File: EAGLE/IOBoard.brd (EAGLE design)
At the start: 160 x 100 mm, 71 parts, among them IC1 MEGA32-P, IC2 MAX232, IC3 ADM803SAKS, K1 HE3321, K2 HE3321, K3 HE3321, K4 HE3321, K5 HE3321, K6 HE3321, K7 HE3321, K8 HE3321, T1 NDS351AN, T2 NDS351AN, T3 NDS351AN, T4 NDS351AN, T5 NDS351AN, T6 NDS351AN, T7 NDS351AN, T8 NDS351AN

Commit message: -
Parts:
- removed D1, D2, D3, D4, D5, D6, D7, D8: 1N4148, diode:DO35-10
- removed IC2: MAX232, maxim:DIL16
- removed IC3: ADM803SAKS, memmert_joerg:SC70-3L
- removed K1, K2, K3, K4, K5, K6, K7, K8: HE3321, relay:HE3321
- removed OK1, OK2, OK3, OK4, OK5, OK6, OK7, OK8: SFH6206, optocoupler:DIL4-SMD
- removed R10, R11, R12, R13, R14, R15, R16: 374, rcl:0207/10
- removed T1, T2, T3, T4, T5, T6, T7, T8: NDS351AN, memmert_joerg:SOT23
- removed X1, X10, X11, X12, X13, X14, X15, X16, X2, X3, X4, X5, X6, X7, X8, X9: (no value), con-phoenix-500:MSTBV2
- removed X17: (no value), con-subd:F09H
- added 3V3, BAT: (no value), pinhead:1X02
- added C3, C4, C5: 100n, rcl:C0805
- added C6, C7, C8, C9: 20p, rcl:C0805
- added JP1: (no value), pinhead:1X09
- added JP10, JP11, JP2, JP3, JP4, JP5, JP6, JP7, JP8, JP9: JUMPER_SMALL, memmert_joerg:JUMPER
- added JTAG: (no value), con-harting-ml:ML20
- added LED1, LED2, LED3, LED4: (no value), led:SML0603
- added Q2: 32kHz, crystal:MC-306
- added S1: COMBICON_1803442, memmert_joerg:COMBICON_1803442
- added U1: STM32F10XRXT6, stm32:TQFP64
- C1, C2: value (none) -> 100n; device rcl:C025_050-025X075 -> rcl:C0805
- IC1: value MEGA32-P -> TPS61097; device atmel:DIL40 -> spfennig:SOT23-DBV
- Q1: value (none) -> 8MHz; device memmert_joerg:HC49/S -> crystal:CSM-7X-DU
- R1: value 5k -> 390; device rcl:0207/10 -> rcl:R0805
- R2, R3, R4: value 5k -> 10k; device rcl:0207/10 -> rcl:R0805
- R5: value 5k -> 0; device rcl:0207/10 -> rcl:R0805
- R6, R7, R8: value 5k -> 500; device rcl:0207/10 -> rcl:R0805
- R9: value 374 -> 500; device rcl:0207/10 -> rcl:R0805
- moved Q1 299.5 mm to (7.62, 19.7), turned to 90 degrees
- moved C2 237.0 mm to (16.5, 28.6), turned to 270 degrees
- moved C1 217.6 mm to (17.1, 10.8), turned to 90 degrees
- moved R8 150.5 mm to (3.17, 6.99)
- moved R7 130.8 mm to (3.17, 4.45)
- moved R6 111.4 mm to (3.17, 1.91)
- moved IC1 78.0 mm to (2.54, -5.08), turned to 0 degrees
- moved R5 65.5 mm to (27.3, 13.3), turned to 270 degrees
- moved R4 36.1 mm to (36.8, 38.1), turned to 90 degrees
- moved R3 20.1 mm to (34.3, 38.1), turned to 90 degrees
- moved R9 12.6 mm to (3.17, 9.53), turned to 0 degrees
- moved R2 12.0 mm to (26.7, 38.1), turned to 90 degrees
- moved R1 7.10 mm to (11.4, 19.7), turned to 270 degrees
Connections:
- removed net IN0: IC1.40, OK1.4, R1.1
- removed net IN1: IC1.39, OK2.4, R2.1
- removed net IN2: IC1.38, OK3.4, R3.1
- removed net IN3: IC1.37, OK4.4, R4.1
- removed net IN4: IC1.36, OK5.4, R5.1
- removed net IN5: IC1.35, OK6.4, R6.1
- removed net IN6: IC1.34, OK7.4, R7.1
- removed net IN7: IC1.33, OK8.4, R8.1
- removed net N$15: OK3.1, R11.2
- removed net N$16: C2.2, IC2.5
- removed net N$17: R13.1, X5.1
- removed net N$18: OK5.2, X5.2
- removed net N$19: D1.A, K1.3, T1.3
- removed net N$20: OK5.1, R13.2
- removed net N$21: R14.1, X6.1
- removed net N$22: OK6.2, X6.2
- removed net N$23: IC1.9, IC3.2
- removed net N$24: OK6.1, R14.2
- removed net N$25: R15.1, X7.1
- removed net N$26: OK7.2, X7.2
- removed net N$27: D4.A, K2.3, T2.3
- removed net N$28: OK7.1, R15.2
- removed net N$29: R16.1, X8.1
- removed net N$30: OK8.2, X8.2
- removed net N$31: D5.A, K3.3, T3.3
- removed net N$32: OK8.1, R16.2
- removed net N$33: D7.A, K4.3, T4.3
- removed net N$34: D2.A, K5.3, T5.3
- removed net N$35: D3.A, K6.3, T6.3
- removed net N$36: D8.A, K8.3, T8.3
- removed net N$37: D6.A, K7.3, T7.3
- removed net N$38: K1.4, X9.2
- removed net N$39: K1.1, X9.1
- removed net N$40: K2.4, X10.2
- removed net N$41: K2.1, X10.1
- removed net N$42: K3.4, X11.2
- removed net N$43: K3.1, X11.1
- removed net N$44: K4.4, X12.2
- removed net N$45: K4.1, X12.1
- removed net N$46: K8.4, X16.2
- removed net N$47: K8.1, X16.1
- removed net N$48: K7.1, X15.1
- removed net N$49: K7.4, X15.2
- removed net N$50: K6.1, X14.1
- removed net N$51: K6.4, X14.2
- removed net N$52: K5.1, X13.1
- removed net N$53: K5.4, X13.2
- removed net N$54: IC2.7, X17.3
- removed net N$55: IC2.13, X17.2
- removed net N$56: IC1.12, Q1.2
- removed net N$57: IC1.13, Q1.1
- removed net OUT0: IC1.1, T1.1
- removed net OUT1: IC1.2, T2.1
- removed net OUT2: IC1.3, T3.1
- removed net OUT3: IC1.4, T4.1
- removed net OUT4: IC1.5, T5.1
- removed net OUT5: IC1.6, T6.1
- removed net OUT6: IC1.7, T7.1
- removed net OUT7: IC1.8, T8.1
- removed net RXUART: IC1.14
- removed net TCK: IC1.24
- removed net TDI: IC1.27
- removed net TDO: IC1.26
- removed net TMS: IC1.25
- removed net TXUART: IC1.15
- removed net VCC: D1.C, D2.C, D3.C, D4.C, D5.C, D6.C, D7.C, D8.C, IC1.10, IC1.30, IC1.32, IC2.16, IC2.2, IC3.3, K1.2, K2.2, K3.2, K4.2, K5.2, K6.2, K7.2, K8.2, R1.2, R2.2, R3.2, R4.2, R5.2, R6.2, R7.2, R8.2
- new net +3V3: 3V3.1, C1.2, C2.2, C3.2, C4.2, IC1.4, JP1.2, JP1.9, JP10.2, JP8.2, JTAG.1, JTAG.2, S1.3, U1.1, U1.13, U1.19, U1.32, U1.48, U1.64
- new net BAT+: BAT.1, IC1.1, IC1.3
- new net BAT-: BAT.2, IC1.2
- new net BOOT0: JP10.1, JP11.1, U1.60
- new net BOOT1: JP8.1, JP9.1, U1.28
- new net JTAG_DBGACK: JTAG.19, R4.2
- new net JTAG_DBGRQ: JTAG.17, R3.2
- new net JTAG_NSRST: JP7.2, JTAG.15
- new net JTAG_NTRST: JP3.2, JTAG.3
- new net JTAG_RTCK: JTAG.11, R2.2
- new net JTAG_TCK: JP4.2, JTAG.9
- new net JTAG_TDI: JP5.2, JTAG.5
- new net JTAG_TDO: JP2.2, JTAG.13
- new net JTAG_TMS: JP6.2, JTAG.7
- new net LCD_CS: JP1.7, U1.58
- new net LCD_D/C: JP1.5, U1.41
- new net LCD_MISO: JP1.1, U1.22
- new net LCD_MOSI: JP1.4, U1.23
- new net LCD_RESET: JP1.6, U1.38
- new net LCD_SCK: JP1.3, U1.21
- new net OSC_RTC_IN: C8.1, Q2.4, U1.35
- new net OSC_RTC_OUT: R5.1, U1.36
- new net SERIAL1_RX: S1.2, U1.43
- new net SERIAL1_TX: S1.1, U1.42
- new net TEST_1: LED1.A, U1.17
- new net TEST_2: LED2.A, U1.16
- new net TEST_3: LED3.A, U1.15
- new net TEST_4: LED4.A, U1.14
- net GND: now also 3V3.2, C1.1, C2.1, C3.1, C4.1, C5.2, C6.2, C7.1, C8.2, C9.1, JP1.8, JP11.2, JP9.2, JTAG.10, JTAG.12, JTAG.14, JTAG.16, JTAG.18, JTAG.20, JTAG.4, JTAG.6, JTAG.8, R2.1, R3.1, R4.1, R6.1, R7.1, R8.1, R9.1, S1.4, U1.12, U1.18, U1.31, U1.47, U1.63; no longer IC1.11, IC1.31, IC2.15, IC2.6, IC3.1, OK1.3, OK2.3, OK3.3, OK4.3, OK5.3, OK6.3, OK7.3, OK8.3, T1.2, T2.2, T3.2, T4.2, T5.2, T6.2, T7.2, T8.2, X17.5
- net N$1: now also C5.1, JP7.1, U1.7; no longer R9.1, X1.1
- net N$10: now also C9.2, Q2.1, R5.2; no longer OK4.2, X4.2
- net N$11: now also LED1.C, R6.2; no longer C2.1, IC2.4
- net N$12: now also LED2.C, R7.2; no longer OK3.2, X3.2
- net N$13: now also LED3.C, R8.2; no longer R12.1, X4.1
- net N$14: now also LED4.C, R9.2; no longer OK4.1, R12.2
- net N$2: now also C6.1, Q1.2, U1.5; no longer OK1.1, R9.2
- net N$3: now also R1.1, U1.6; no longer C1.1, IC2.1
- net N$4: now also JP2.1, U1.55; no longer OK1.2, X1.2
- net N$5: now also C7.2, Q1.1, R1.2; no longer R10.1, X2.1
- net N$6: now also JP4.1, U1.49; no longer OK2.1, R10.2
- net N$7: now also JP6.1, U1.46; no longer OK2.2, X2.2
- net N$8: now also JP5.1, U1.50; no longer C1.2, IC2.3
- net N$9: now also JP3.1, U1.56; no longer R11.1, X3.1
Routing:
- net GND: track 373.4 -> 29.0 mm, vias 0 -> 22
- net VCC: track 162.6 -> 0.00 mm
- net +3V3: track 0.00 -> 136.9 mm, vias 0 -> 1
- net IN7: track 84.1 -> 0.00 mm
- net IN0: track 74.0 -> 0.00 mm
- net IN6: track 63.8 -> 0.00 mm
- net IN1: track 53.6 -> 0.00 mm
- net IN5: track 43.5 -> 0.00 mm
- net LCD_CS: track 0.00 -> 34.5 mm
- net IN2: track 33.3 -> 0.00 mm
- net BOOT0: track 0.00 -> 31.8 mm, vias 0 -> 2
- net N$1: track 6.39 -> 37.7 mm, vias 0 -> 3
- net SERIAL1_TX: track 0.00 -> 30.1 mm
- net LCD_MISO: track 0.00 -> 26.2 mm, vias 0 -> 1
- net IN4: track 23.2 -> 0.00 mm
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- added copper zone on layer 16, net GND
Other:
- board size 160 x 100 mm -> 50 x 50 mm
- board text added: "x"

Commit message: -
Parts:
- added C10, C11: 10u, rcl:C0805
- added L2: 4u7, ipc-7351-inductor:INDC6350X200N
- moved BAT 44.5 mm to (3.17, 47.6), turned to 180 degrees
- moved IC1 40.1 mm to (5.08, 34.9), turned to 270 degrees
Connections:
- new net N$15: IC1.5, L2.2
- net +3V3: now also C11.2
- net BAT+: now also C10.2, L2.1
- net BAT-: now also C10.1
- net GND: now also C11.1
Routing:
- net BAT+: track 0.00 -> 20.9 mm
- net BAT-: track 0.00 -> 15.6 mm
- net +3V3: track 136.9 -> 144.6 mm
- net N$15: track 0.00 -> 6.47 mm
- net GND: track 29.0 -> 29.6 mm, vias 22 -> 23

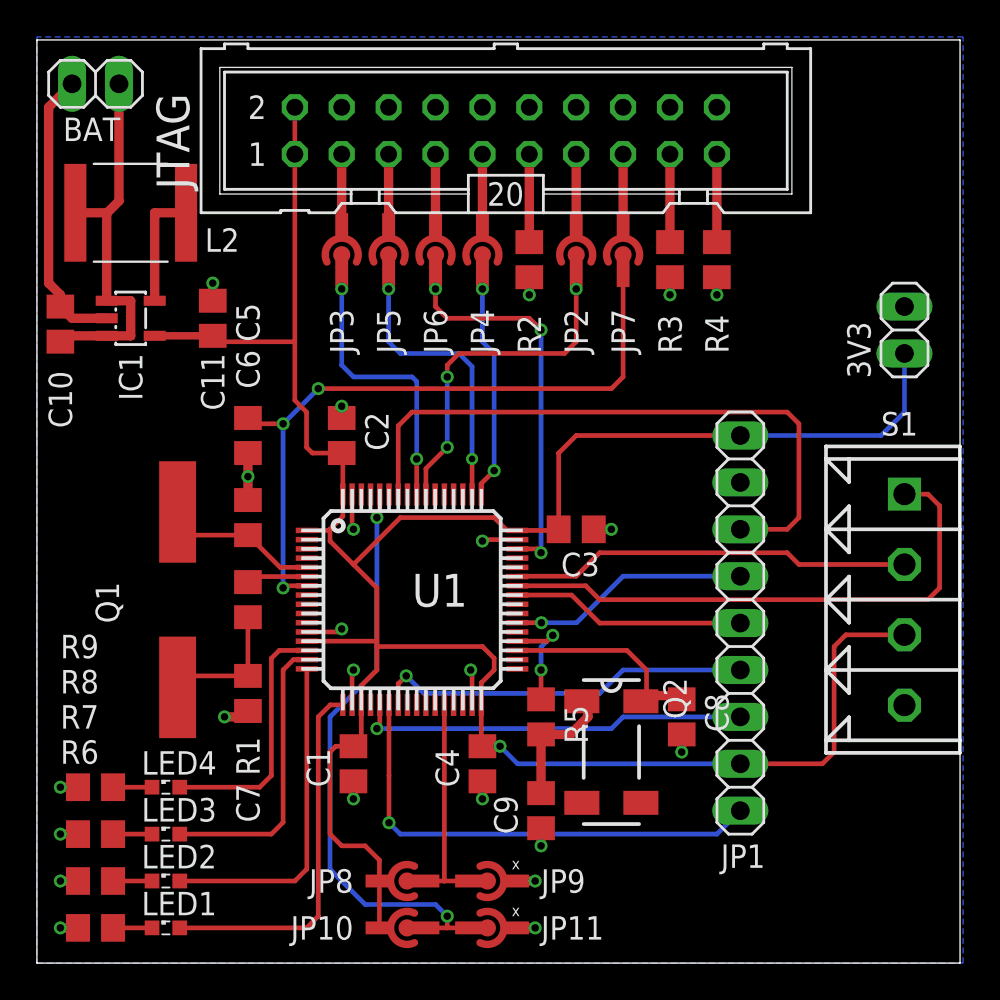
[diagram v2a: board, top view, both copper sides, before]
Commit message: Added +3.3V plane to circuit board.
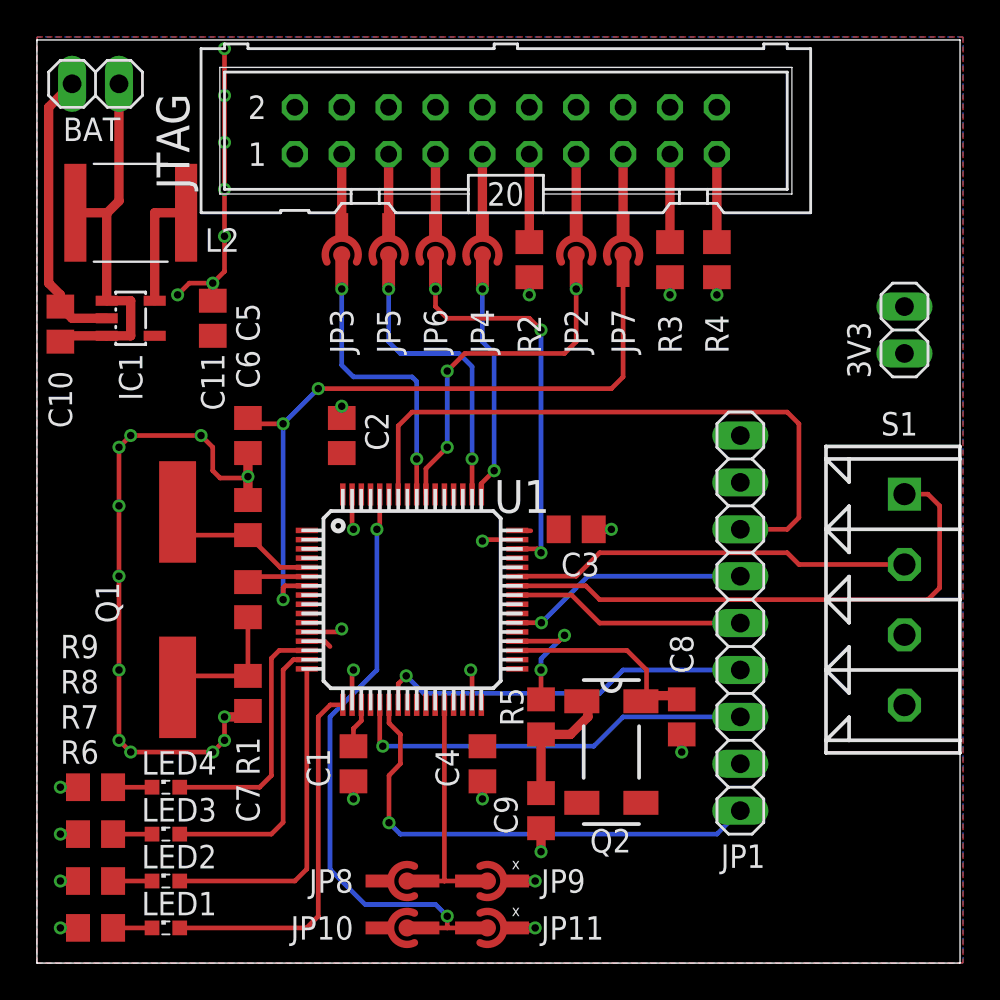
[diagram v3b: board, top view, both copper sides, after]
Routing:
- net +3V3: track 144.6 -> 4.53 mm, vias 1 -> 0
- net GND: track 29.6 -> 77.3 mm, vias 23 -> 39
- net N$1: track 37.3 -> 38.6 mm
- net LCD_SCK: track 21.3 -> 22.3 mm
- net OSC_RTC_OUT: track 5.78 -> 6.68 mm
- net LCD_MISO: track 26.2 -> 26.7 mm
- added copper zone on layer 1, net +3V3

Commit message: Fixed bug with NAN
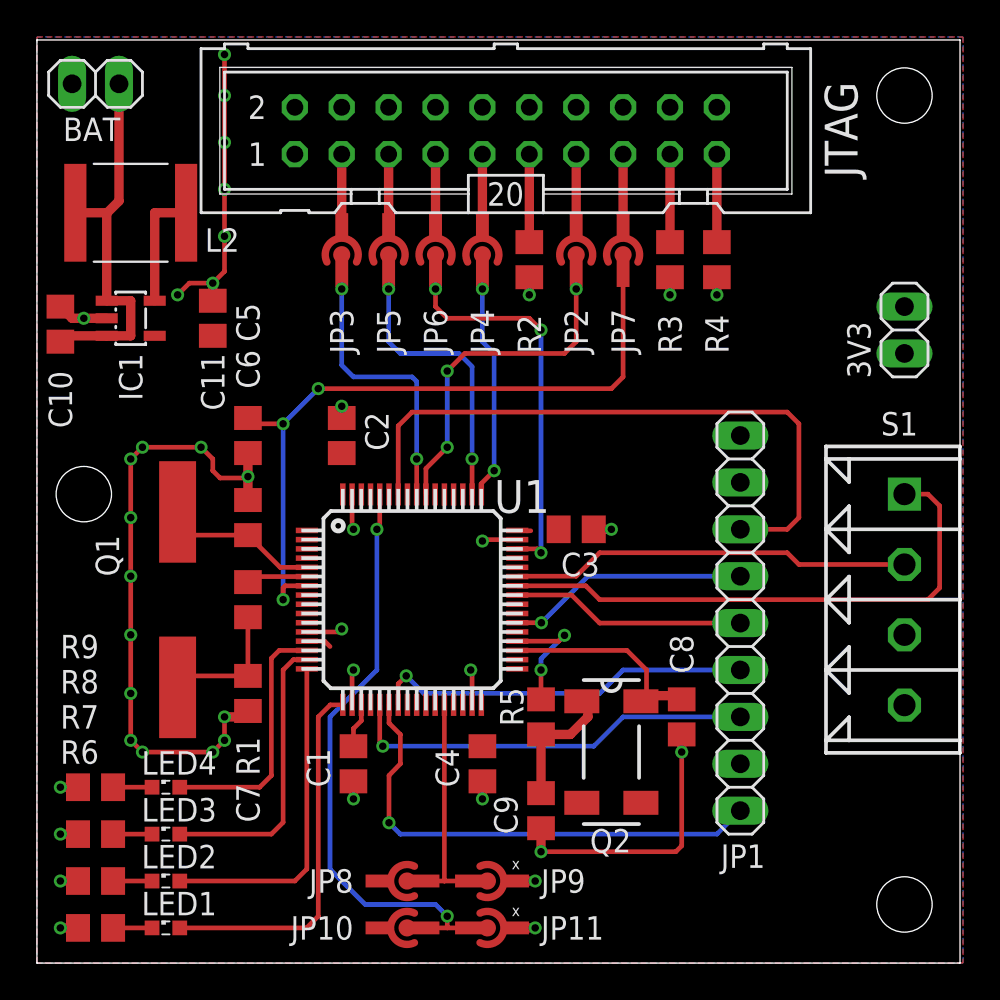
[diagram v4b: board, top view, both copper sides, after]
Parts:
- C8, C9: value 20p -> 10p
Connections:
- removed net BAT-: BAT.2, C10.1, IC1.2
- net GND: now also BAT.2, C10.1, IC1.2
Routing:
- net BAT-: track 15.6 -> 0.00 mm
- net GND: track 77.3 -> 90.1 mm, vias 39 -> 41
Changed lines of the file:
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@@
 <setting verticaltext="up"/>
 </settings>
-<grid distance="25" unitdist="mil" unit="mil" style="lines" multiple="1" display="yes" altdistance="3.125" altunitdist="mil" altunit="mil"/>
+<grid distance="25" unitdist="mil" unit="mm" style="lines" multiple="1" display="yes" altdistance="12.5" altunitdist="mil" altunit="mil"/>
 <layers>
 <layer number="1" name="Top" color="4" fill="1" visible="yes" active="yes"/>
@@
 <text x="25.7175" y="5.08" size="0.6096" layer="21">x</text>
 <text x="25.7175" y="2.54" size="0.6096" layer="21">x</text>
+<hole x="46.99" y="46.99" drill="3"/>
+<hole x="46.99" y="3.175" drill="3"/>
+<hole x="2.54" y="25.4" drill="3"/>
 </plain>
 <attributes>
@@
 <attribute name="MF" value="" x="7.62" y="19.685" size="1.778" layer="27" rot="R90" display="off"/>
 <attribute name="OC_FARNELL" value="unknown" x="7.62" y="19.685" size="1.778" layer="27" rot="R90" display="off"/>
-<attribute name="NAME" x="4.4516" y="18.4062" size="1.27" layer="25" rot="R90"/>
+<attribute name="NAME" x="4.4516" y="20.9462" size="1.27" layer="25" rot="R90"/>
 <attribute name="VALUE" x="11.9314" y="12.0562" size="1.27" layer="27" rot="R90"/>
 </element>
@@
 <attribute name="MF" value="" x="25.4" y="45.085" size="1.778" layer="27" display="off"/>
 <attribute name="OC_FARNELL" value="unknown" x="25.4" y="45.085" size="1.778" layer="27" display="off"/>
-<attribute name="NAME" x="8.255" y="41.91" size="1.778" layer="25" ratio="10" rot="R90"/>
+<attribute name="NAME" x="44.45" y="42.545" size="1.778" layer="25" ratio="10" rot="R90"/>
 <attribute name="VALUE" x="26.67" y="50.165" size="1.778" layer="27" ratio="10"/>
 </element>
@@
 <attribute name="VALUE" x="26.522" y="15.4492" size="1.27" layer="27" rot="R270"/>
 </element>
-<element name="C8" library="rcl" package="C0805" value="20p" x="34.925" y="13.335" smashed="yes" rot="R270">
+<element name="C8" library="rcl" package="C0805" value="10p" x="34.925" y="13.335" smashed="yes" rot="R270">
 <attribute name="NAME" x="34.29" y="17.78" size="1.27" layer="25" rot="R270"/>
 <attribute name="VALUE" x="32.385" y="14.605" size="1.27" layer="27" rot="R270"/>
 </element>
-<element name="C9" library="rcl" package="C0805" value="20p" x="27.305" y="8.255" smashed="yes" rot="R90">
+<element name="C9" library="rcl" package="C0805" value="10p" x="27.305" y="8.255" smashed="yes" rot="R90">
 <attribute name="NAME" x="26.035" y="6.985" size="1.27" layer="25" rot="R90"/>
 <attribute name="VALUE" x="29.845" y="6.985" size="1.27" layer="27" rot="R90"/>
@@
 <wire x1="11.350625" y1="26.273125" x2="9.921875" y2="26.273125" width="0.254" layer="1"/>
 <wire x1="9.921875" y1="26.273125" x2="9.525" y2="26.67" width="0.254" layer="1"/>
-<wire x1="9.525" y1="26.67" x2="9.525" y2="27.94" width="0.254" layer="1"/>
-<wire x1="9.525" y1="27.94" x2="8.89" y2="28.575" width="0.254" layer="1"/>
-<wire x1="8.89" y1="28.575" x2="5.08" y2="28.575" width="0.254" layer="1"/>
-<wire x1="5.08" y1="28.575" x2="4.445" y2="27.94" width="0.254" layer="1"/>
-<wire x1="4.445" y1="27.94" x2="4.445" y2="24.765" width="0.254" layer="1"/>
-<wire x1="4.445" y1="24.765" x2="4.445" y2="20.955" width="0.254" layer="1"/>
-<wire x1="4.445" y1="20.955" x2="4.445" y2="15.875" width="0.254" layer="1"/>
-<wire x1="4.445" y1="15.875" x2="4.445" y2="12.065" width="0.254" layer="1"/>
-<wire x1="4.445" y1="12.065" x2="5.08" y2="11.43" width="0.254" layer="1"/>
-<wire x1="5.08" y1="11.43" x2="9.525" y2="11.43" width="0.254" layer="1"/>
+<wire x1="9.525" y1="26.67" x2="9.525" y2="27.305" width="0.254" layer="1"/>
+<wire x1="9.525" y1="27.305" x2="8.89" y2="27.94" width="0.254" layer="1"/>
+<wire x1="8.89" y1="27.94" x2="5.715" y2="27.94" width="0.254" layer="1"/>
+<wire x1="5.715" y1="27.94" x2="5.08" y2="27.305" width="0.254" layer="1"/>
+<wire x1="5.08" y1="27.305" x2="5.08" y2="24.13" width="0.254" layer="1"/>
+<wire x1="5.08" y1="24.13" x2="5.08" y2="20.955" width="0.254" layer="1"/>
+<wire x1="5.08" y1="20.955" x2="5.08" y2="17.78" width="0.254" layer="1"/>
+<wire x1="5.08" y1="17.78" x2="5.08" y2="14.605" width="0.254" layer="1"/>
+<wire x1="5.08" y1="14.605" x2="5.08" y2="12.065" width="0.254" layer="1"/>
+<wire x1="5.08" y1="12.065" x2="5.715" y2="11.43" width="0.254" layer="1"/>
+<wire x1="5.715" y1="11.43" x2="9.525" y2="11.43" width="0.254" layer="1"/>
 <wire x1="9.525" y1="11.43" x2="10.16" y2="12.065" width="0.254" layer="1"/>
 <wire x1="10.16" y1="12.065" x2="10.16" y2="13.335" width="0.254" layer="1"/>
-<wire x1="10.16" y1="49.53" x2="10.16" y2="46.99" width="0.254" layer="1"/>
+<wire x1="10.16" y1="49.2125" x2="10.16" y2="46.99" width="0.254" layer="1"/>
 <wire x1="10.16" y1="46.99" x2="10.16" y2="44.45" width="0.254" layer="1"/>
 <wire x1="10.16" y1="44.45" x2="10.16" y2="41.91" width="0.254" layer="1"/>
@@
 <wire x1="8.255" y1="36.83" x2="7.62" y2="36.195" width="0.254" layer="1"/>
 <via x="7.62" y="36.195" extent="1-16" drill="0.4064"/>
-<via x="10.16" y="49.53" extent="1-16" drill="0.4064"/>
+<via x="10.16" y="49.2125" extent="1-16" drill="0.4064"/>
 <via x="10.16" y="46.99" extent="1-16" drill="0.4064"/>
 <via x="10.16" y="44.45" extent="1-16" drill="0.4064"/>
 <via x="10.16" y="41.91" extent="1-16" drill="0.4064"/>
 <via x="10.16" y="39.37" extent="1-16" drill="0.4064"/>
-<via x="8.89" y="28.575" extent="1-16" drill="0.4064"/>
-<via x="5.08" y="28.575" extent="1-16" drill="0.4064"/>
-<via x="4.445" y="27.94" extent="1-16" drill="0.4064"/>
-<via x="4.445" y="24.765" extent="1-16" drill="0.4064"/>
-<via x="4.445" y="20.955" extent="1-16" drill="0.4064"/>
-<via x="4.445" y="15.875" extent="1-16" drill="0.4064"/>
-<via x="4.445" y="12.065" extent="1-16" drill="0.4064"/>
-<via x="5.08" y="11.43" extent="1-16" drill="0.4064"/>
+<via x="8.89" y="27.94" extent="1-16" drill="0.4064"/>
+<via x="5.715" y="27.94" extent="1-16" drill="0.4064"/>
+<via x="5.08" y="27.305" extent="1-16" drill="0.4064"/>
+<via x="5.08" y="24.13" extent="1-16" drill="0.4064"/>
+<via x="5.08" y="20.955" extent="1-16" drill="0.4064"/>
+<via x="5.08" y="14.605" extent="1-16" drill="0.4064"/>
+<via x="5.08" y="12.065" extent="1-16" drill="0.4064"/>
+<via x="5.715" y="11.43" extent="1-16" drill="0.4064"/>
 <via x="9.525" y="11.43" extent="1-16" drill="0.4064"/>
 <via x="10.16" y="12.065" extent="1-16" drill="0.4064"/>
+<contactref element="IC1" pad="2"/>
+<contactref element="C10" pad="1"/>
+<wire x1="1.27" y1="35.5575" x2="1.9025" y2="34.925" width="0.508" layer="1"/>
+<wire x1="1.9025" y1="34.925" x2="2.54" y2="34.925" width="0.508" layer="1"/>
+<contactref element="BAT" pad="2"/>
+<wire x1="2.54" y1="34.925" x2="3.78" y2="34.925" width="0.508" layer="1"/>
+<via x="2.54" y="34.925" extent="1-16" drill="0.4064"/>
+<wire x1="27.305" y1="6.0325" x2="34.6075" y2="6.0325" width="0.254" layer="1"/>
+<wire x1="34.6075" y1="6.0325" x2="34.925" y2="6.35" width="0.254" layer="1"/>
+<wire x1="34.925" y1="6.35" x2="34.925" y2="11.43" width="0.254" layer="1"/>
+<via x="5.08" y="17.78" extent="1-16" drill="0.4064"/>
 </signal>
 <signal name="+3V3">
@@
 <wire x1="3.81" y1="40.64" x2="3.78" y2="40.64" width="0.508" layer="1"/>
 </signal>
-<signal name="BAT-">
-<contactref element="BAT" pad="2"/>
-<contactref element="IC1" pad="2"/>
-<contactref element="C10" pad="1"/>
-<wire x1="1.27" y1="35.5575" x2="1.9025" y2="34.925" width="0.508" layer="1"/>
-<wire x1="1.9025" y1="34.925" x2="3.78" y2="34.925" width="0.508" layer="1"/>
-<wire x1="1.905" y1="47.625" x2="0.635" y2="46.355" width="0.508" layer="1"/>
-<wire x1="0.635" y1="46.355" x2="0.635" y2="36.83" width="0.508" layer="1"/>
-<wire x1="0.635" y1="36.83" x2="1.27" y2="36.195" width="0.508" layer="1"/>
-<wire x1="1.27" y1="36.195" x2="1.27" y2="35.5575" width="0.508" layer="1"/>
-</signal>
 <signal name="N$15">
